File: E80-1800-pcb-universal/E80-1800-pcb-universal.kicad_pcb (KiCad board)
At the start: 2 copper layers, 382 x 160 mm, 330 parts, among them J1 SPI, J2 BATT, J3 OLED, J4 USB_C_Receptacle_USB2.0, Q1 AO3400A, SW1 RST, SW2 BOOT, U1 SRV05-4, U2 XC6206P332MR, U3 STM32F072RBTx

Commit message: moved graphics
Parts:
- added G***: LOGO, keygem_branding:keygem_logo_mask_15, B.Cu at (183.4, 19.1)
- moved G*** 11.3 mm to (213.4, 19.0)
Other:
- board text added: "E80-1800 KEYGEM-Edition r1 github.com/ebastler/E80-1800 KEYGEM.store mpwr.xyz"
- board text removed: "E80-1800 github.com/ebastler/E80-1800 mpwr.xyz"

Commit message: moved graphics
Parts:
- removed the G*** at (183.4, 19.1)
- moved G*** 13.3 mm to (226.7, 19.0)
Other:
- board text added: "E80-1800 r1 github.com/ebastler/E80-1800 mpwr.xyz"
- board text removed: "E80-1800 KEYGEM-Edition r1 github.com/ebastler/E80-1800 KEYGEM.store mpwr.xyz"

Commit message: minor routing changes, exposed copper for usb traces, added TVS
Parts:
- added D1: BSD3C051V, Diode_SMD:D_SOD-323, B.Cu at (324.4, -20.7)
- moved J3 7.62 mm to (257.3, -18.5), turned to 180 degrees
- moved R2 7.61 mm to (260.9, -26.1)
- moved R1 2.56 mm to (260.9, -23.6)
- moved L1 0.06 mm to (322.3, -20.7)
- renumbered D9 to D10, D10 to D11, D11 to D12, D12 to D13, D13 to D14, D14 to D15, D15 to D16, D16 to D17, D17 to D18, D18 to D19, D1 to D2, D19 to D20, D20 to D21, D21 to D22, D22 to D23, D23 to D24, D24 to D25, D25 to D26, D26 to D27, D27 to D28, D28 to D29, D2 to D3, D29 to D30, D30 to D31, D31 to D32, D32 to D33, D33 to D34, D34 to D35, D35 to D36, D36 to D37, D37 to D38, D38 to D39, D3 to D4, D39 to D40, D40 to D41, D41 to D42, D42 to D43, D43 to D44, D44 to D45, D45 to D46, D46 to D47, D47 to D48, D48 to D49, D4 to D5, D49 to D50, D50 to D51, D51 to D52, D52 to D53, D53 to D54, D54 to D55, D55 to D56, D56 to D57, D57 to D58, D5 to D6, D6 to D7, D7 to D8, D8 to D9
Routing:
- net COL00: track 427.4 -> 435.1 mm
- net I2C_SDA: track 39.7 -> 35.2 mm
- net COL01: track 386.1 -> 389.4 mm
- net COL02: track 381.6 -> 384.7 mm
- net COL03: track 335.5 -> 338.5 mm
- net COL14: track 189.3 -> 191.3 mm
- net COL04: track 316.0 -> 317.9 mm
- net COL05: track 299.2 -> 301.0 mm
- net /RST: track 349.8 -> 351.4 mm
- net COL06: track 332.3 -> 333.8 mm
- net COL07: track 272.5 -> 273.9 mm
- net /BOOT: track 378.5 -> 379.9 mm
- net +3V3: track 489.2 -> 490.3 mm
- net COL08: track 253.2 -> 254.3 mm
- net USB-D-: track 47.6 -> 46.6 mm
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
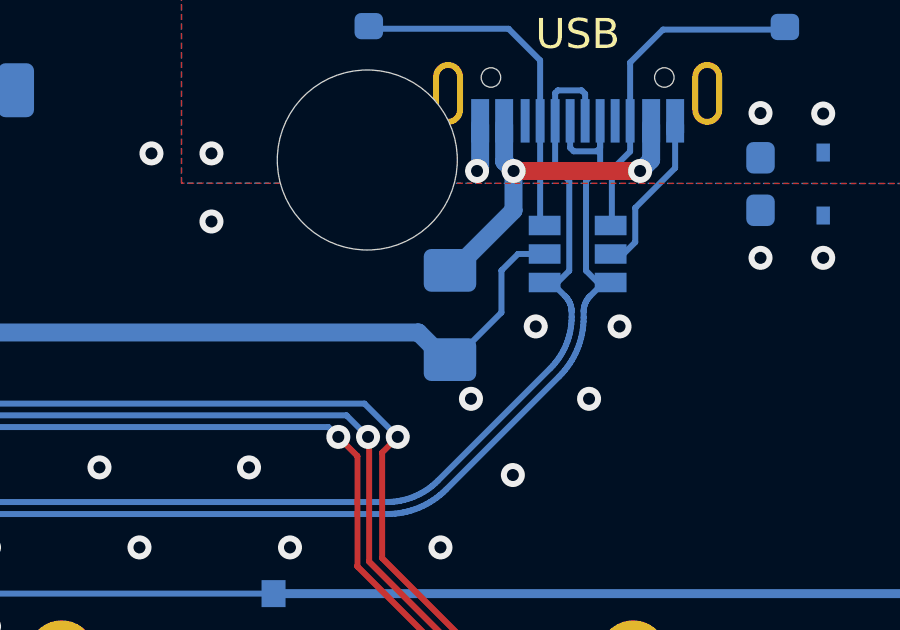
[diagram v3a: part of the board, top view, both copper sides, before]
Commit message: swapped parts to fit jlc stocks
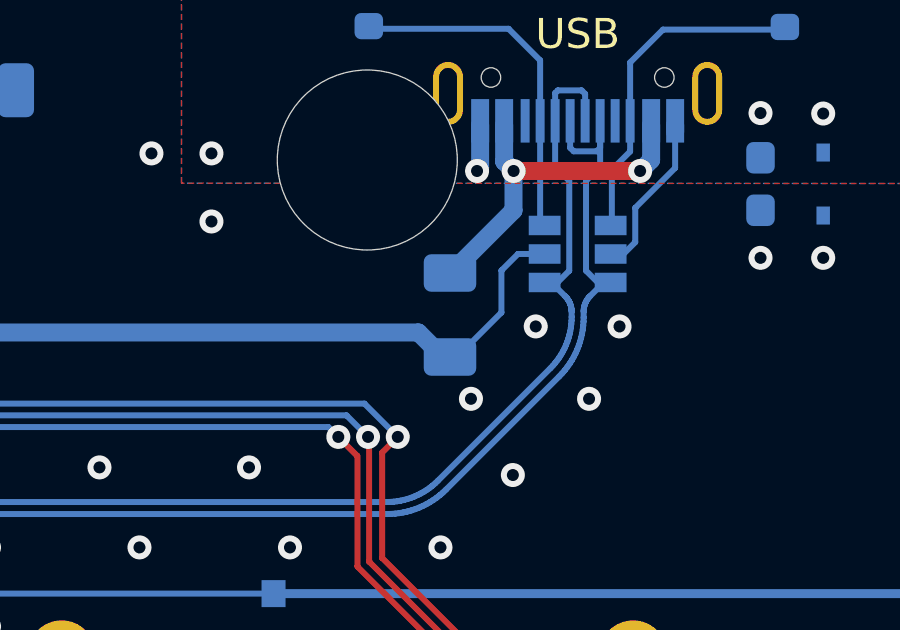
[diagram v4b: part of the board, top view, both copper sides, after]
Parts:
- F1: value SCF075-1206R -> 1206L050; footprint Fuse:Fuse_1206_3216Metric_Pad1.42x1.75mm_HandSolder -> Fuse:Fuse_1206_3216Metric
